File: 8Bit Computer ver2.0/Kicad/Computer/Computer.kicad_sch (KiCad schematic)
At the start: 0 parts

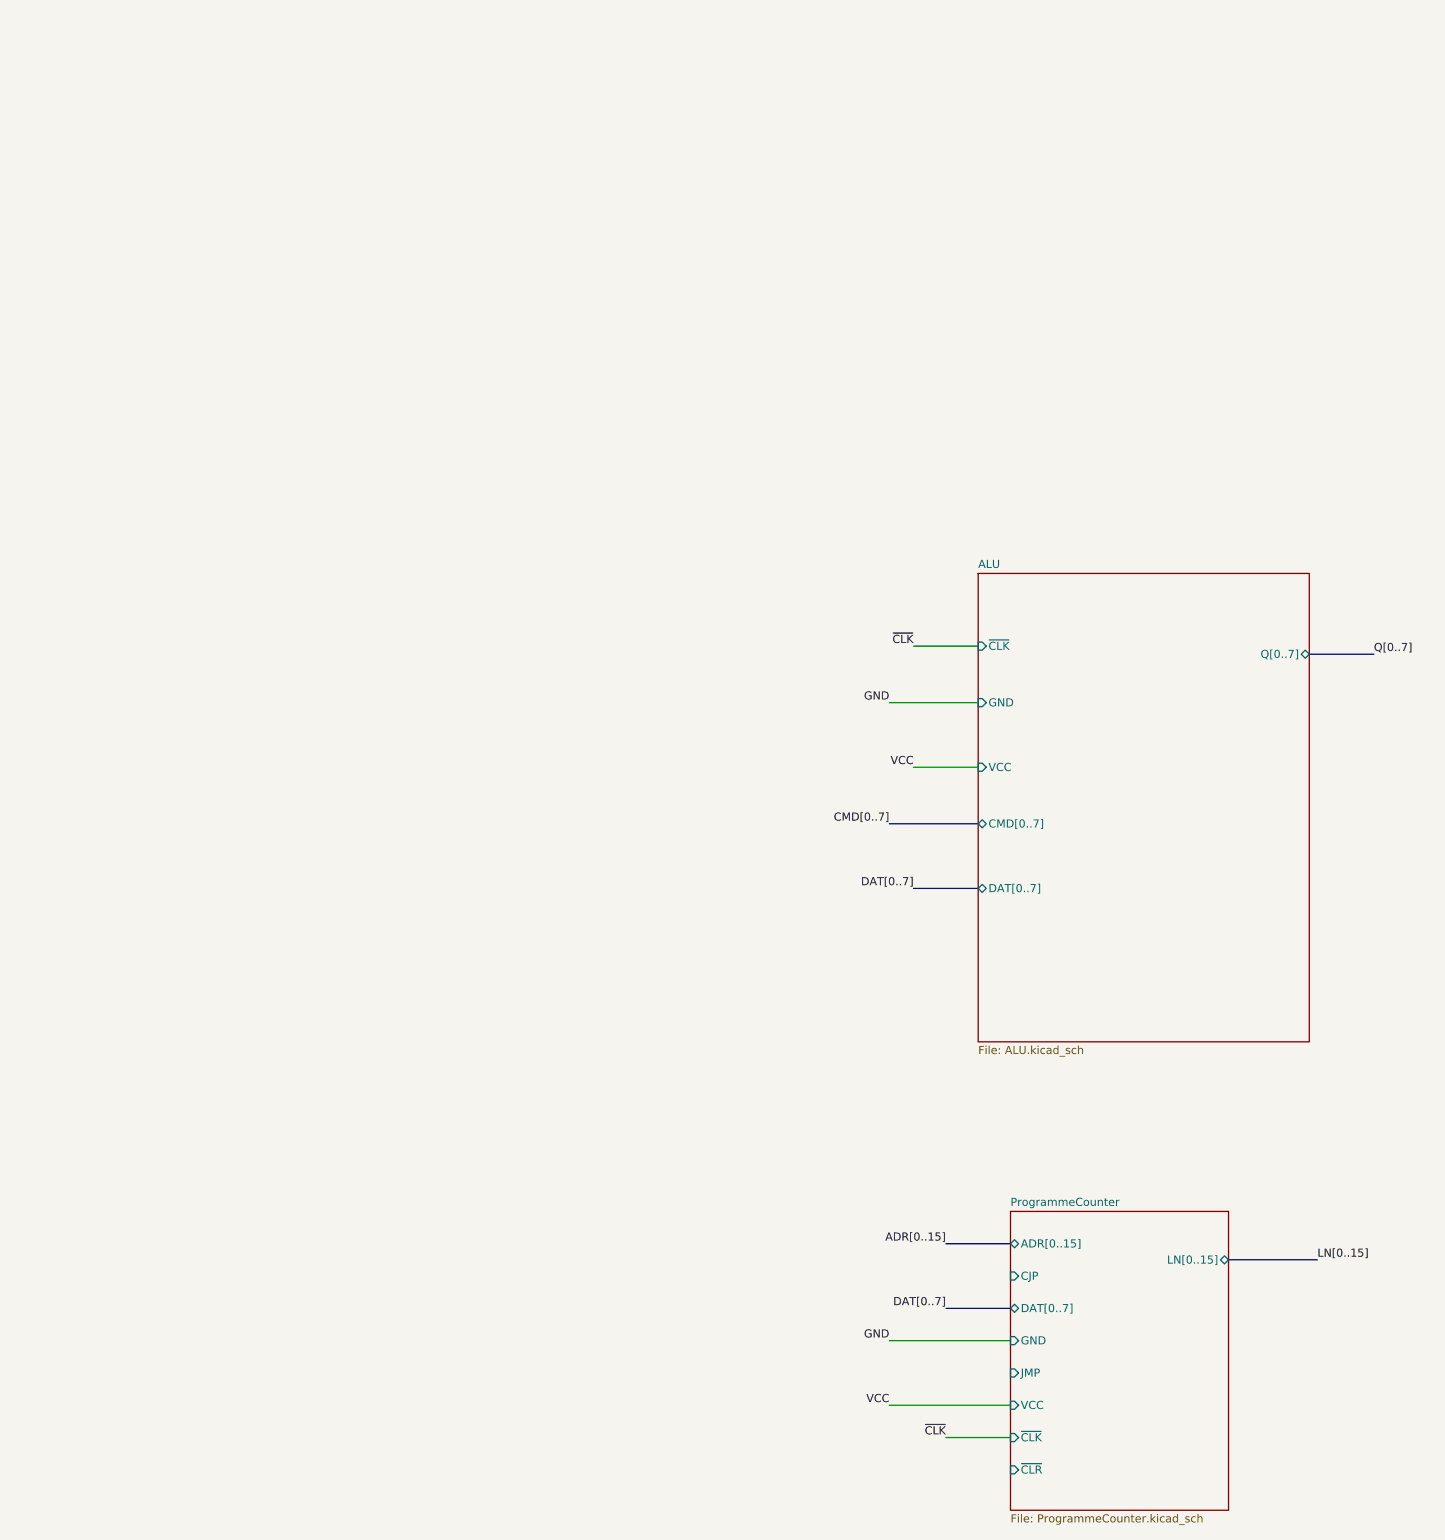
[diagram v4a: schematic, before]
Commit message: Kicad
deleted the Qs
began with FlashMemory
added the CMD comparators for Inc, Comp, AddSub, FlagReg, BarrelShifter, ProgCount
added Diodes and DATdis line
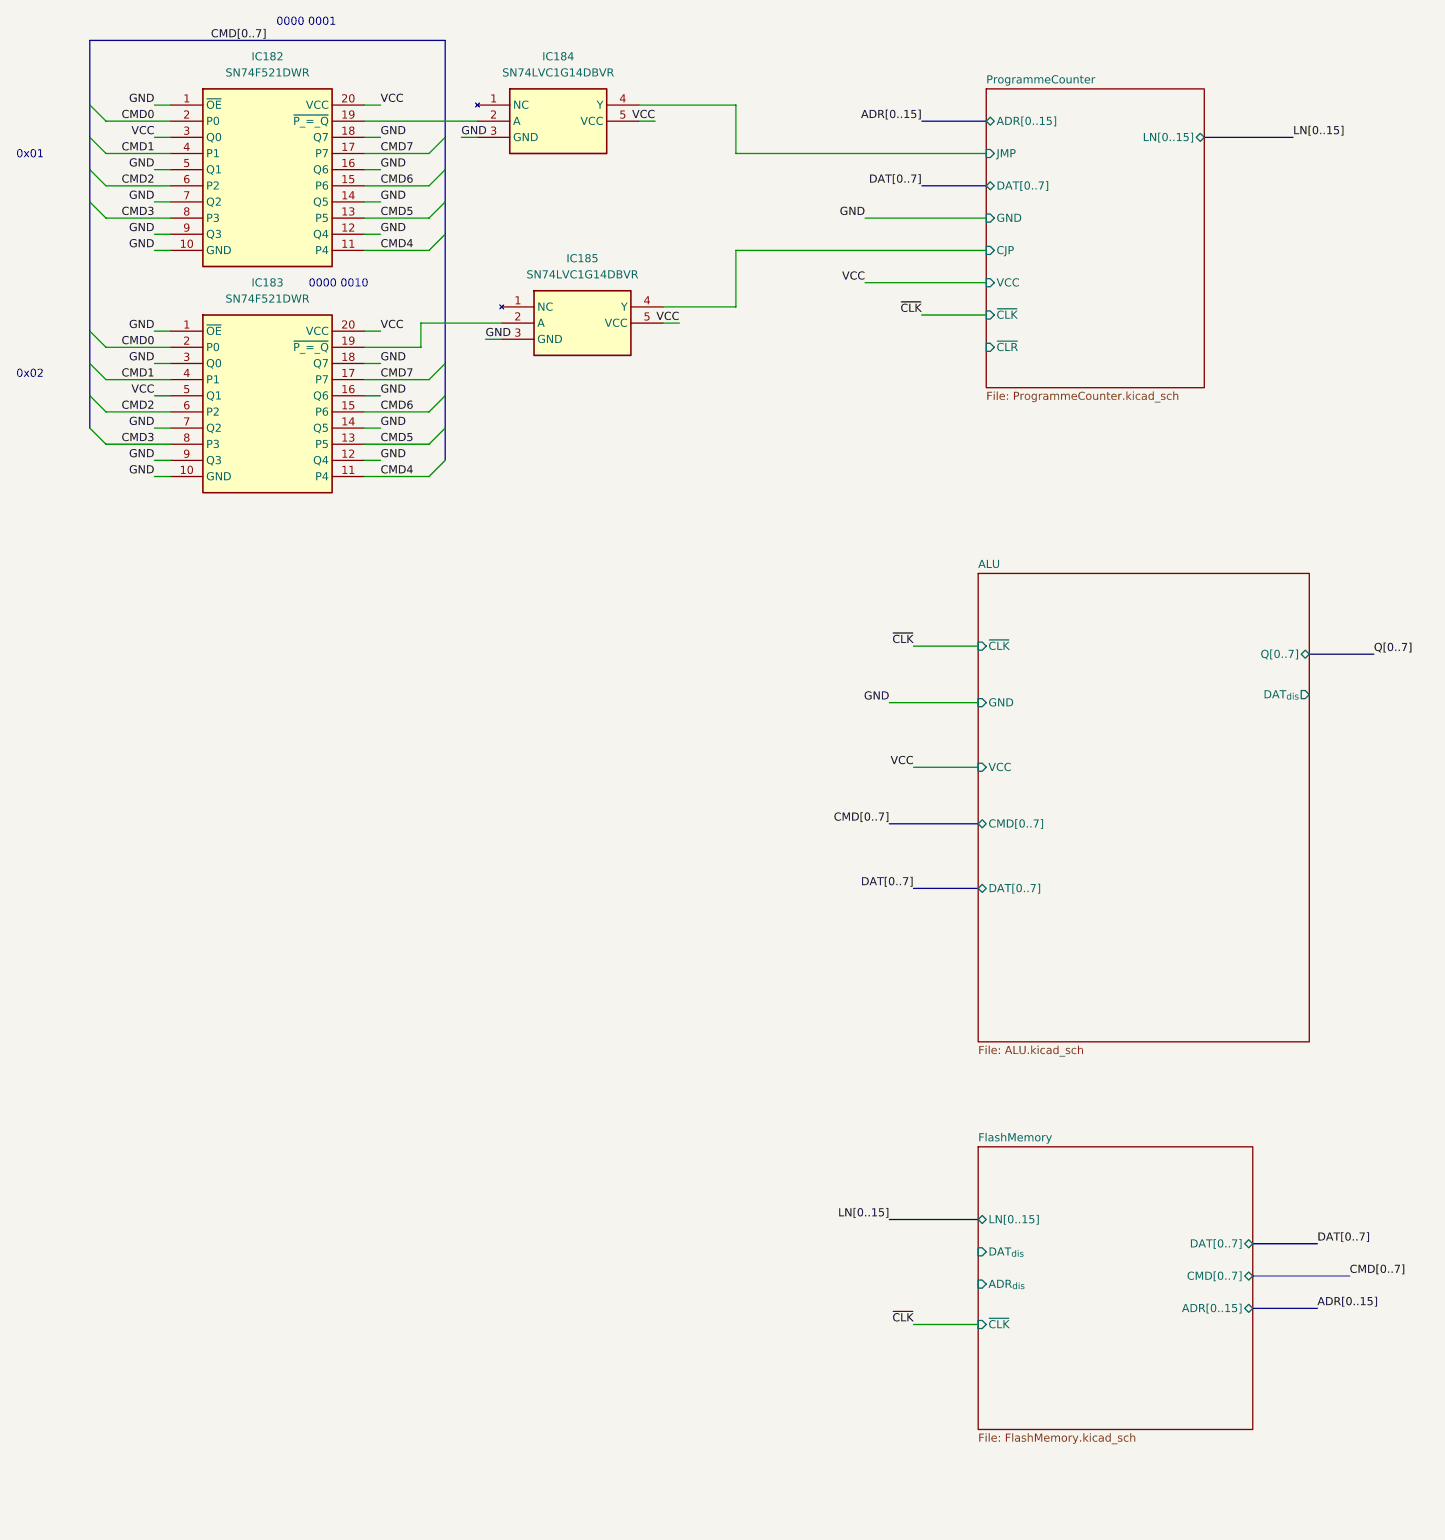
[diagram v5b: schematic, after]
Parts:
- added IC182, IC183: SN74F521DWR, Samacsys:SOIC127P1030X265-20N, symbol Samacsys:SN74F521DWR
- added IC184, IC185: SN74LVC1G14DBVR, Samacsys:SOT95P280X145-5N, symbol Samacsys:SN74LVC1G14DBVR
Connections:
- net GND: now also IC182.1 (~{OE}), IC182.10 (GND), IC182.12 (Q4), IC182.14 (Q5), IC182.16 (Q6), IC182.18 (Q7), IC182.5 (Q1), IC182.7 (Q2), IC182.9 (Q3), IC183.1 (~{OE}), IC183.10 (GND), IC183.12 (Q4), IC183.14 (Q5), IC183.16 (Q6), IC183.18 (Q7), IC183.3 (Q0), IC183.7 (Q2), IC183.9 (Q3), IC184.3 (GND), IC185.3 (GND)
- net ProgrammeCounter/CJP: now also IC185.4 (Y)
- net ProgrammeCounter/JMP: now also IC184.4 (Y)
- net VCC: now also IC182.20 (VCC), IC182.3 (Q0), IC183.20 (VCC), IC183.5 (Q1), IC184.5 (VCC), IC185.5 (VCC)
- new net: IC183.19 (~{P_=_Q}), IC185.2 (A)
- new net: IC182.19 (~{P_=_Q}), IC184.2 (A)
- new net CMD0: IC182.2 (P0), IC183.2 (P0)
- new net CMD1: IC182.4 (P1), IC183.4 (P1)
- new net CMD2: IC182.6 (P2), IC183.6 (P2)
- new net CMD3: IC182.8 (P3), IC183.8 (P3)
- new net CMD4: IC182.11 (P4), IC183.11 (P4)
- new net CMD5: IC182.13 (P5), IC183.13 (P5)
- new net CMD6: IC182.15 (P6), IC183.15 (P6)
- new net CMD7: IC182.17 (P7), IC183.17 (P7)
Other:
- added sheet FlashMemory (FlashMemory.kicad_sch)
- sheet ALU ports: added DAT_{dis}; removed none
- note added: "0000 0001"
- note added: "0000 0010"
- note added: "0x01"
- note added: "0x02"

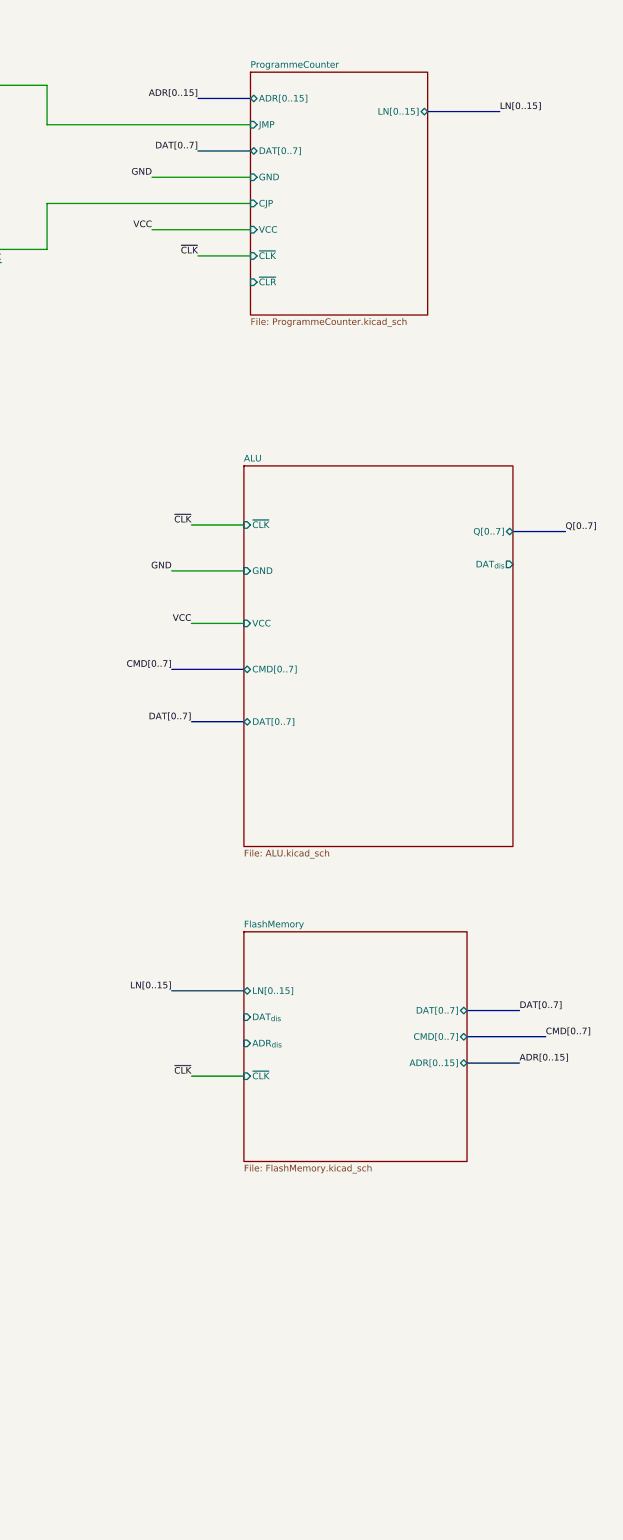
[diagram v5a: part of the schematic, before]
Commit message: Kicad,parts
Kicad:
worked on Flash memory
began RAM
parts:
added Delay Chip for Flash
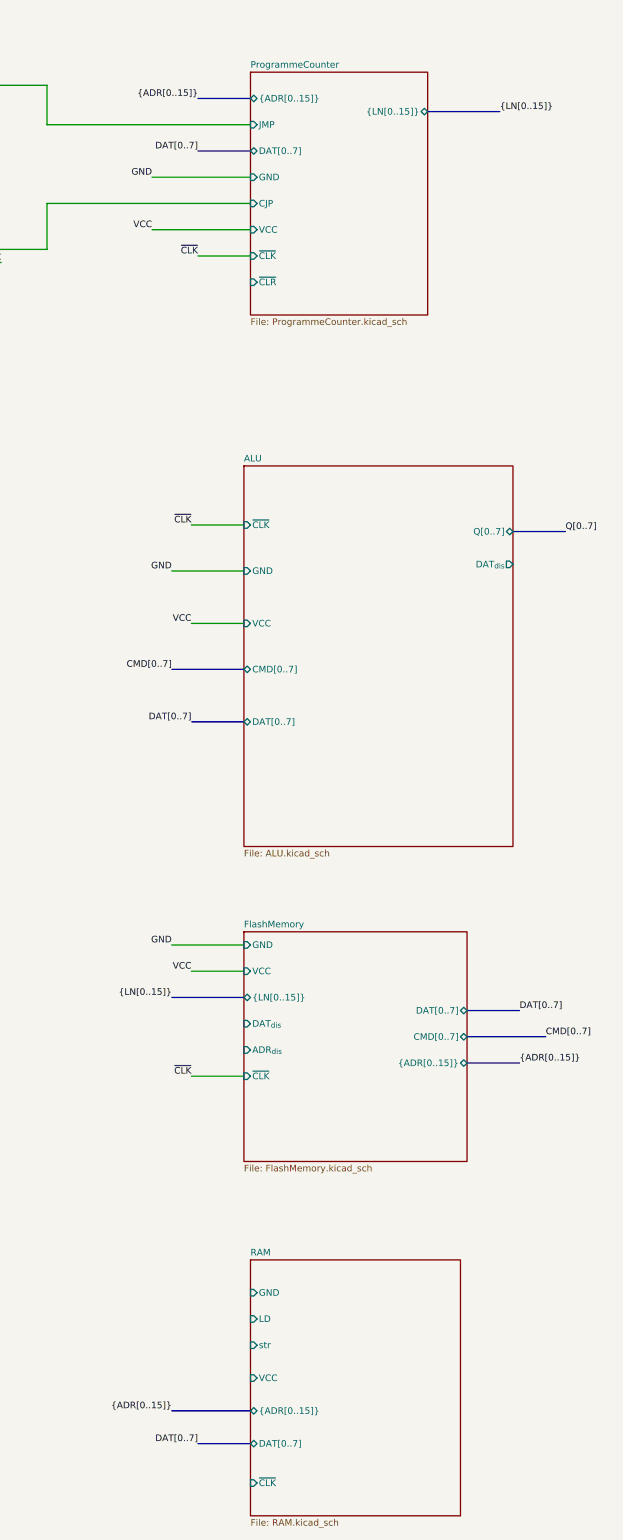
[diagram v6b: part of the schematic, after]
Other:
- added sheet RAM (RAM.kicad_sch)
- sheet FlashMemory ports: added GND, VCC, {ADR[0..15]}, {LN[0..15]}; removed ADR[0..15], LN[0..15]
- sheet ProgrammeCounter ports: added {ADR[0..15]}, {LN[0..15]}; removed ADR[0..15], LN[0..15]
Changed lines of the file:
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@@
+	(wire
+		(pts
+			(xy 457.2 256.54) (xy 467.36 256.54)
+		)
+		(stroke
+			(width 0)
+			(type default)
+		)
+	)
 	(wire
 		(pts
@@
 	(bus
 		(pts
+			(xy 468.63 347.98) (xy 458.47 347.98)
+		)
+		(stroke
+			(width 0)
+			(type default)
+		)
+	)
+	(bus
+		(pts
 			(xy 510.54 274.32) (xy 520.7 274.32)
 		)
@@
 	(bus
 		(pts
-			(xy 453.39 260.35) (xy 467.36 260.35)
+			(xy 453.39 261.62) (xy 467.36 261.62)
 		)
 		(stroke
@@
 		)
 	)
+	(bus
+		(pts
+			(xy 453.39 341.63) (xy 468.63 341.63)
+		)
+		(stroke
+			(width 0)
+			(type default)
+		)
+	)
 	(wire
 		(pts
@@
 		(pts
 			(xy 330.2 123.19) (xy 340.36 123.19)
+		)
+		(stroke
+			(width 0)
+			(type default)
+		)
+	)
+	(wire
+		(pts
+			(xy 453.39 251.46) (xy 467.36 251.46)
 		)
 		(stroke
@@
 		)
 	)
-	(label "LN[0..15]"
-		(at 453.39 260.35 180)
+	(label "{LN[0..15]}"
+		(at 453.39 261.62 180)
 		(effects
 			(font
@@
 		)
 	)
+	(label "DAT[0..7]"
+		(at 458.47 347.98 180)
+		(effects
+			(font
+				(size 1.27 1.27)
+			)
+			(justify right bottom)
+		)
+	)
 	(label "CMD5"
 		(at 373.38 102.87 0)
@@
 		)
 	)
+	(label "GND"
+		(at 453.39 251.46 180)
+		(effects
+			(font
+				(size 1.27 1.27)
+			)
+			(justify right bottom)
+		)
+	)
 	(label "VCC"
 		(at 373.38 85.09 0)
@@
 		)
 	)
-	(label "ADR[0..15]"
+	(label "{ADR[0..15]}"
 		(at 458.47 87.63 180)
 		(effects
@@
 		)
 	)
+	(label "VCC"
+		(at 457.2 256.54 180)
+		(effects
+			(font
+				(size 1.27 1.27)
+			)
+			(justify right bottom)
+		)
+	)
+	(label "{ADR[0..15]}"
+		(at 453.39 341.63 180)
+		(effects
+			(font
+				(size 1.27 1.27)
+			)
+			(justify right bottom)
+		)
+	)
 	(label "GND"
 		(at 337.82 135.89 180)
@@
 		)
 	)
-	(label "LN[0..15]"
+	(label "{LN[0..15]}"
 		(at 516.89 90.17 0)
 		(effects
@@
 		)
 	)
-	(label "ADR[0..15]"
+	(label "{ADR[0..15]}"
 		(at 520.7 274.32 0)
 		(effects
@@
 	)
 	(sheet
+		(at 468.63 312.42)
+		(size 40.64 49.53)
+		(exclude_from_sim no)
+		(in_bom yes)
+		(on_board yes)
+		(dnp no)
+		(fields_autoplaced yes)
+		(stroke
+			(width 0.1524)
+			(type solid)
+		)
+		(fill
+			(color 0 0 0 0.0000)
+		)
+		(property "Sheetname" "RAM"
+			(at 468.63 311.7084 0)
+			(effects
+				(font
+					(size 1.27 1.27)
+				)
+				(justify left bottom)
+			)
+		)
+		(property "Sheetfile" "RAM.kicad_sch"
+			(at 468.63 362.5346 0)
+			(effects
+				(font
+					(size 1.27 1.27)
+				)
+				(justify left top)
+			)
+		)
+		(pin "GND" input
+			(at 468.63 318.77 180)
+			(effects
+				(font
+					(size 1.27 1.27)
+				)
+				(justify left)
+			)
+		)
+		(pin "LD" input
+			(at 468.63 323.85 180)
+			(effects
+				(font
+					(size 1.27 1.27)
+				)
+				(justify left)
+			)
+		)
+		(pin "str" input
+			(at 468.63 328.93 180)
+			(effects
+				(font
+					(size 1.27 1.27)
+				)
+				(justify left)
+			)
+		)
+		(pin "VCC" input
+			(at 468.63 335.28 180)
+			(effects
+				(font
+					(size 1.27 1.27)
+				)
+				(justify left)
+			)
+		)
+		(pin "{ADR[0..15]}" tri_state
+			(at 468.63 341.63 180)
+			(effects
+				(font
+					(size 1.27 1.27)
+				)
+				(justify left)
+			)
+		)
+		(pin "DAT[0..7]" tri_state
+			(at 468.63 347.98 180)
+			(effects
+				(font
+					(size 1.27 1.27)
+				)
+				(justify left)
+			)
+		)
+		(pin "~{CLK}" input
+			(at 468.63 355.6 180)
+			(effects
+				(font
+					(size 1.27 1.27)
+				)
+				(justify left)
+			)
+		)
+		(instances
+			(project "Computer"
+				(path "/1196a00e-6878-4d6d-82b7-9e052dfe7c14"
+					(page "18")
+				)
+			)
+		)
+	)
+	(sheet
 		(at 467.36 248.92)
 		(size 43.18 44.45)
@@
 			)
 		)
-		(pin "ADR[0..15]" tri_state
+		(pin "ADR_{dis}" input
+			(at 467.36 271.78 180)
+			(effects
+				(font
+					(size 1.27 1.27)
+				)
+				(justify left)
+			)
+		)
+		(pin "DAT_{dis}" input
+			(at 467.36 266.7 180)
+			(effects
+				(font
+					(size 1.27 1.27)
+				)
+				(justify left)
+			)
+		)
+		(pin "~{CLK}" input
+			(at 467.36 276.86 180)
+			(effects
+				(font
+					(size 1.27 1.27)
+				)
+				(justify left)
+			)
+		)
+		(pin "GND" input
+			(at 467.36 251.46 180)
+			(effects
+				(font
+					(size 1.27 1.27)
+				)
+				(justify left)
+			)
+		)
+		(pin "VCC" input
+			(at 467.36 256.54 180)
+			(effects
+				(font
+					(size 1.27 1.27)
+				)
+				(justify left)
+			)
+		)
+		(pin "{ADR[0..15]}" tri_state
 			(at 510.54 274.32 0)
 			(effects
@@
 				)
 				(justify right)
-			)
-		)
-		(pin "ADR_{dis}" input
-			(at 467.36 270.51 180)
-			(effects
-				(font
-					(size 1.27 1.27)
-				)
-				(justify left)
 			)
 		)
@@
 			)
 		)
-		(pin "DAT_{dis}" input
-			(at 467.36 265.43 180)
-			(effects
-				(font
-					(size 1.27 1.27)
-				)
-				(justify left)
-			)
-		)
-		(pin "~{CLK}" input
-			(at 467.36 276.86 180)
-			(effects
-				(font
-					(size 1.27 1.27)
-				)
-				(justify left)
-			)
-		)
-		(pin "LN[0..15]" tri_state
-			(at 467.36 260.35 180)
+		(pin "{LN[0..15]}" tri_state
+			(at 467.36 261.62 180)
 			(effects
 				(font
@@
 			)
 		)
-		(pin "ADR[0..15]" tri_state
+		(pin "{ADR[0..15]}" tri_state
 			(at 468.63 87.63 180)
 			(effects
@@
 			)
 		)
-		(pin "LN[0..15]" tri_state
+		(pin "{LN[0..15]}" tri_state
 			(at 502.92 90.17 0)
 			(effects
